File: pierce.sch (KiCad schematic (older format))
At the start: 81 parts, among them J1 Conn_01x10, J2 Conn_01x10, J3 Trackpoint, SW1 SW_PUSH, SW10 SW_PUSH, SW11 SW_PUSH, SW12 SW_PUSH, SW13 SW_PUSH, SW14 SW_PUSH, SW15 SW_PUSH, SW16 SW_PUSH, SW17 SW_PUSH, SW18 SW_PUSH, SW19 SW_PUSH, SW2 SW_PUSH, SW20 SW_PUSH, SW21 SW_PUSH, SW22 SW_PUSH, SW23 SW_PUSH, SW24 SW_PUSH, SW25 SW_PUSH, SW26 SW_PUSH, SW27 SW_PUSH, SW28 SW_PUSH, SW29 SW_PUSH, SW3 SW_PUSH, SW30 SW_PUSH, SW31 SW_PUSH, SW32 SW_PUSH, SW33 SW_PUSH, SW34 SW_PUSH, SW35 SW_PUSH, SW36 SW_PUSH, SW37 SW_PUSH, SW4 SW_PUSH, SW5 SW_PUSH, SW6 SW_PUSH, SW7 SW_PUSH, SW8 SW_PUSH, SW9 SW_PUSH, U1 ProMicro_r

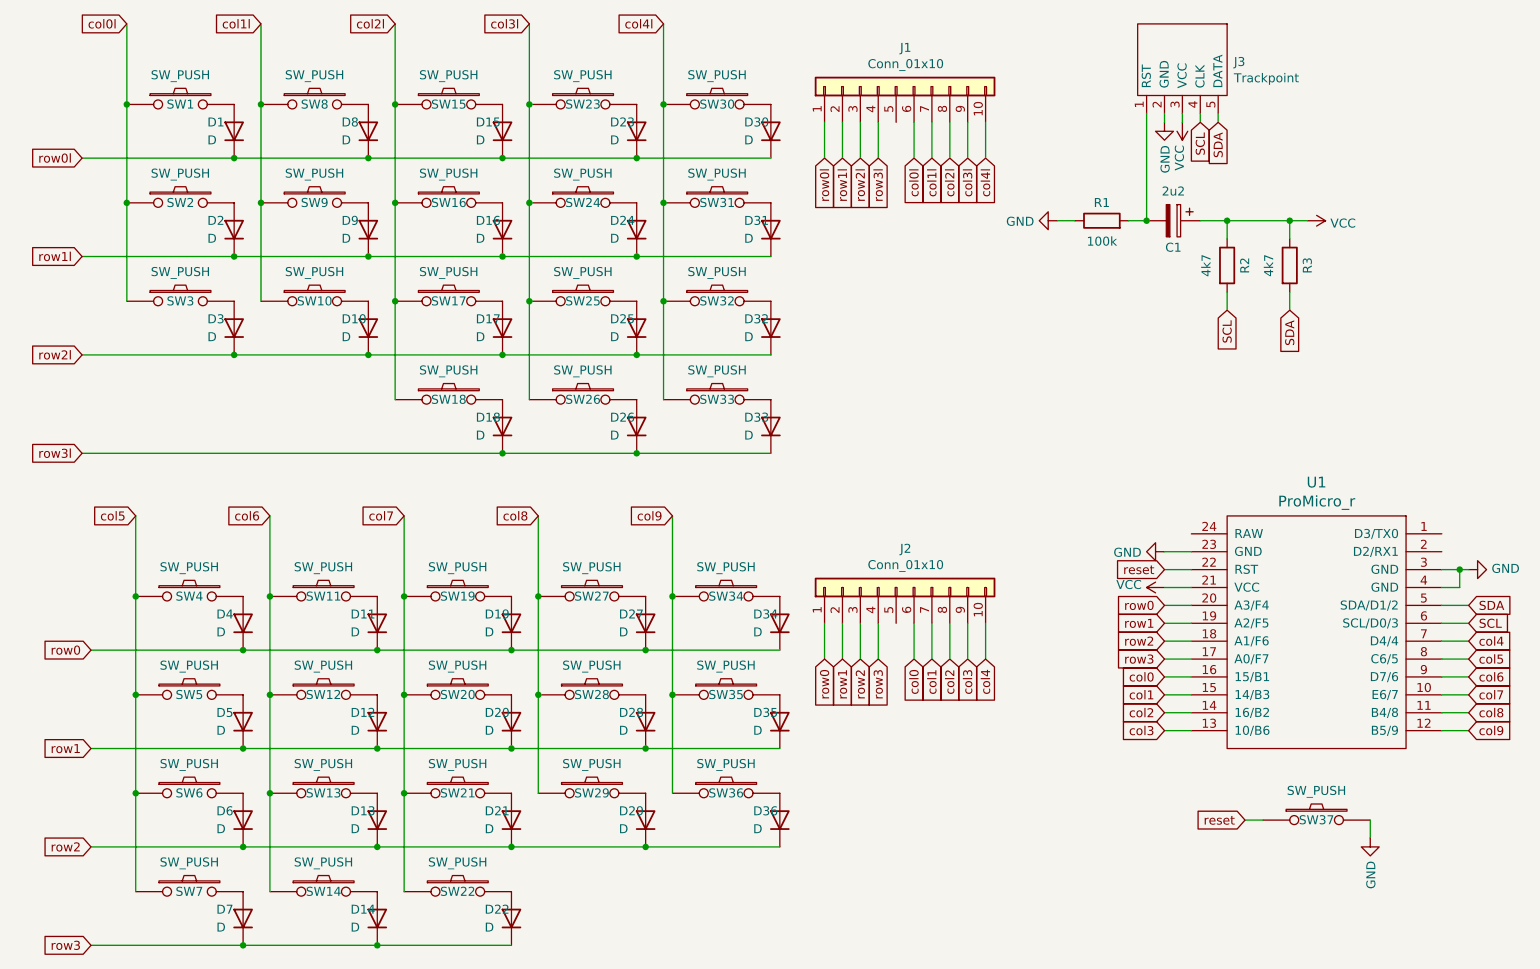
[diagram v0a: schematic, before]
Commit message: Finished routing (improved routing from last commit)
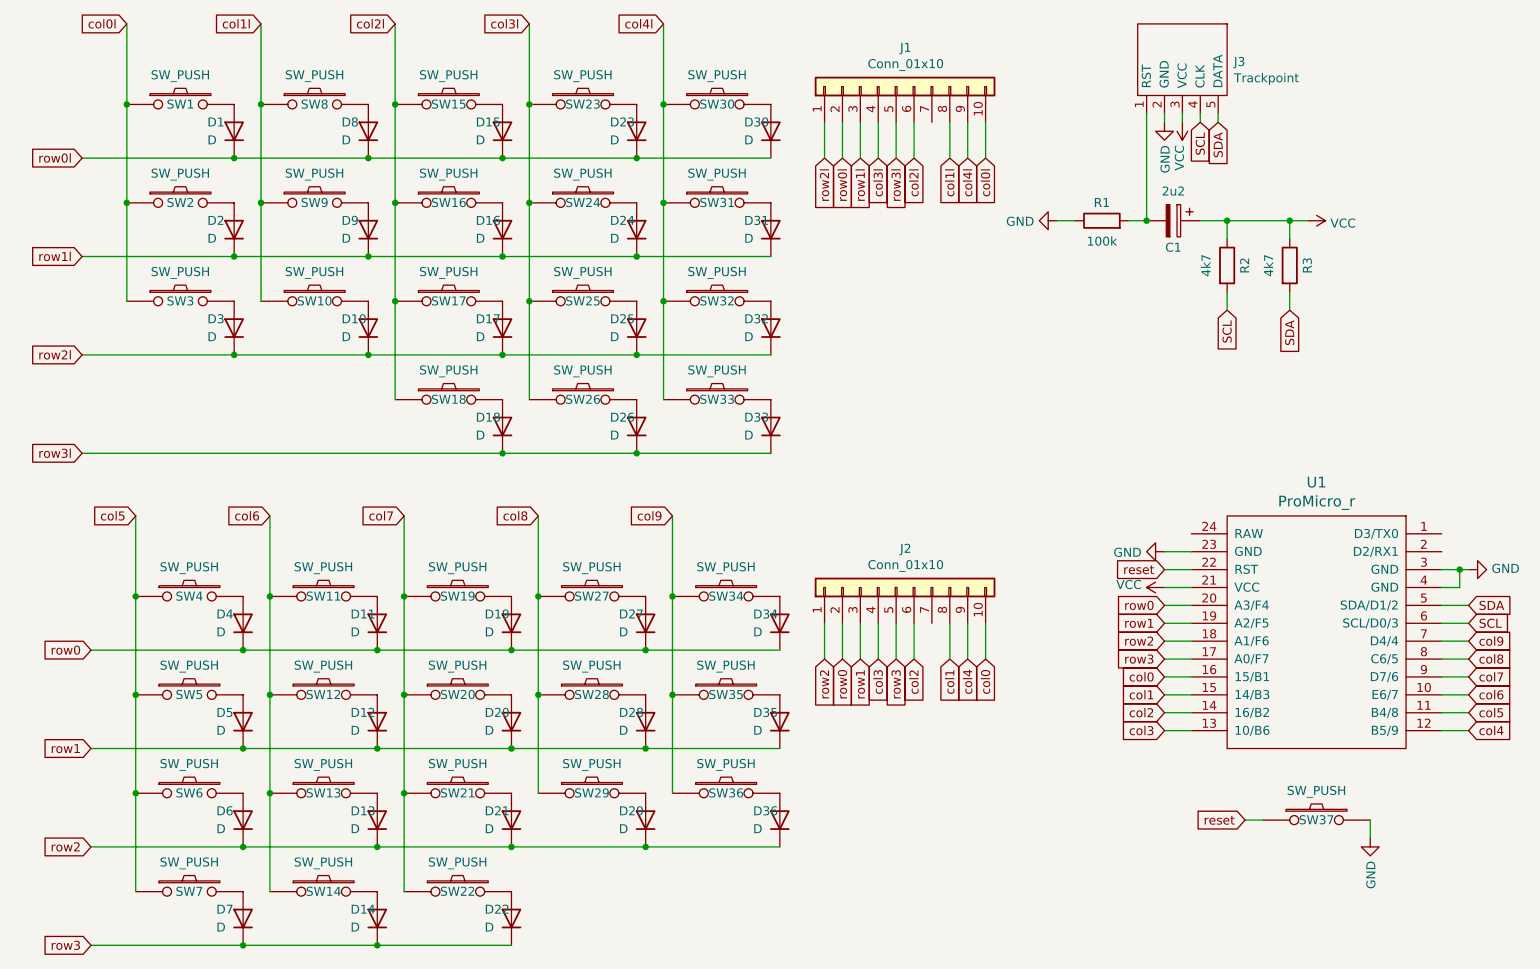
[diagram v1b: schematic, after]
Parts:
- SW1, SW10, SW11, SW12, SW13, SW14, SW15, SW16, SW17, SW18, SW19, SW2, SW20, SW21, SW22, SW23, SW24, SW25, SW26, SW27, SW28, SW29, SW3, SW30, SW31, SW32, SW33, SW34, SW35, SW36, SW4, SW5, SW6, SW7, SW8, SW9: footprint kbd:CherryMX_Hotswap -> kbd:CherryMX_ChocV2_1u
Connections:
- net col0: now also J2.10 (Pin_10); no longer J2.6 (Pin_6)
- net col0l: now also J1.10 (Pin_10); no longer J1.6 (Pin_6)
- net col1: now also J2.8 (Pin_8); no longer J2.7 (Pin_7)
- net col1l: now also J1.8 (Pin_8); no longer J1.7 (Pin_7)
- net col2: now also J2.6 (Pin_6); no longer J2.8 (Pin_8)
- net col2l: now also J1.6 (Pin_6); no longer J1.8 (Pin_8)
- net col3: now also J2.4 (Pin_4); no longer J2.9 (Pin_9)
- net col3l: now also J1.4 (Pin_4); no longer J1.9 (Pin_9)
- net col4: now also J2.9 (Pin_9), U1.12 (B5/9); no longer J2.10 (Pin_10), U1.7 (D4/4)
- net col4l: now also J1.9 (Pin_9); no longer J1.10 (Pin_10)
- net col5: now also U1.11 (B4/8); no longer U1.8 (C6/5)
- net col6: now also U1.10 (E6/7); no longer U1.9 (D7/6)
- net col7: now also U1.9 (D7/6); no longer U1.10 (E6/7)
- net col8: now also U1.8 (C6/5); no longer U1.11 (B4/8)
- net col9: now also U1.7 (D4/4); no longer U1.12 (B5/9)
- net row0: now also J2.2 (Pin_2); no longer J2.1 (Pin_1)
- net row0l: now also J1.2 (Pin_2); no longer J1.1 (Pin_1)
- net row1: now also J2.3 (Pin_3); no longer J2.2 (Pin_2)
- net row1l: now also J1.3 (Pin_3); no longer J1.2 (Pin_2)
- net row2: now also J2.1 (Pin_1); no longer J2.3 (Pin_3)
- net row2l: now also J1.1 (Pin_1); no longer J1.3 (Pin_3)
- net row3: now also J2.5 (Pin_5); no longer J2.4 (Pin_4)
- net row3l: now also J1.5 (Pin_5); no longer J1.4 (Pin_4)
